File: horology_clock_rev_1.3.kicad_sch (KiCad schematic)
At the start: 49 parts, among them J1 Conn_01x36, J10 Conn_01x08, J11 Screw_Terminal_01x02, J12 Conn_01x02, J13 Conn_01x04, J14 Conn_01x10, J2 Conn_01x36, J3 Screw_Terminal_01x02, J4 Screw_Terminal_01x02, J5 Screw_Terminal_01x02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

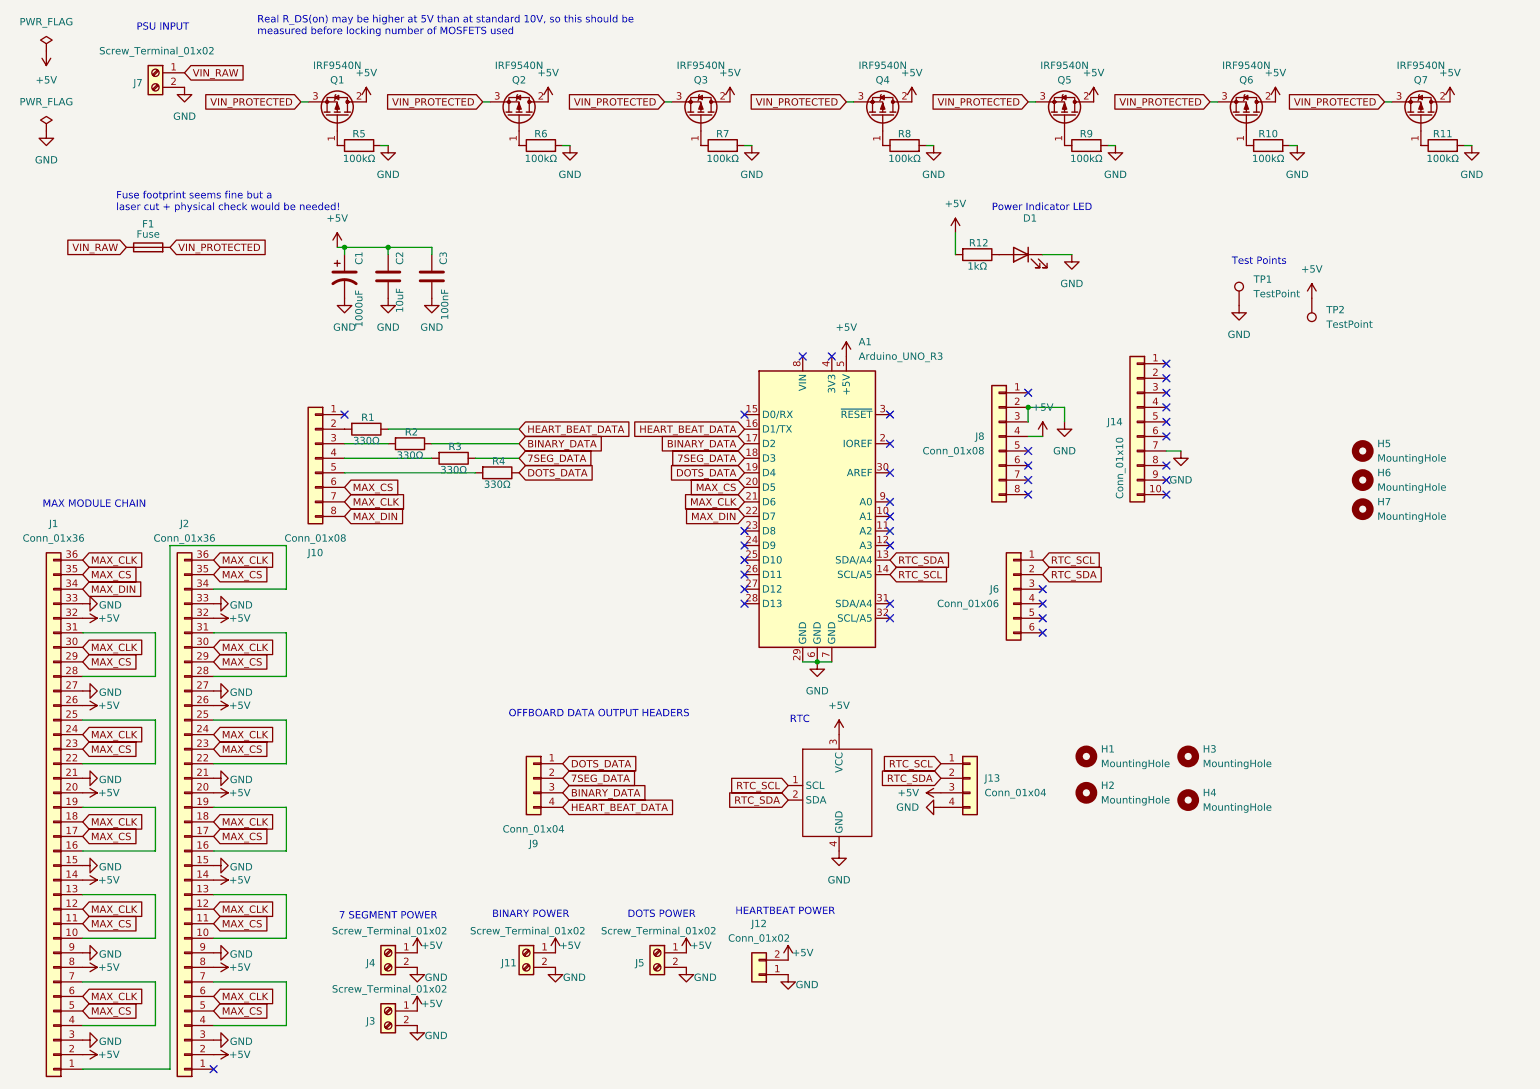
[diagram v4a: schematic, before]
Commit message: Moved Pin 1 to Pin 8 to avoid Serial Issues.
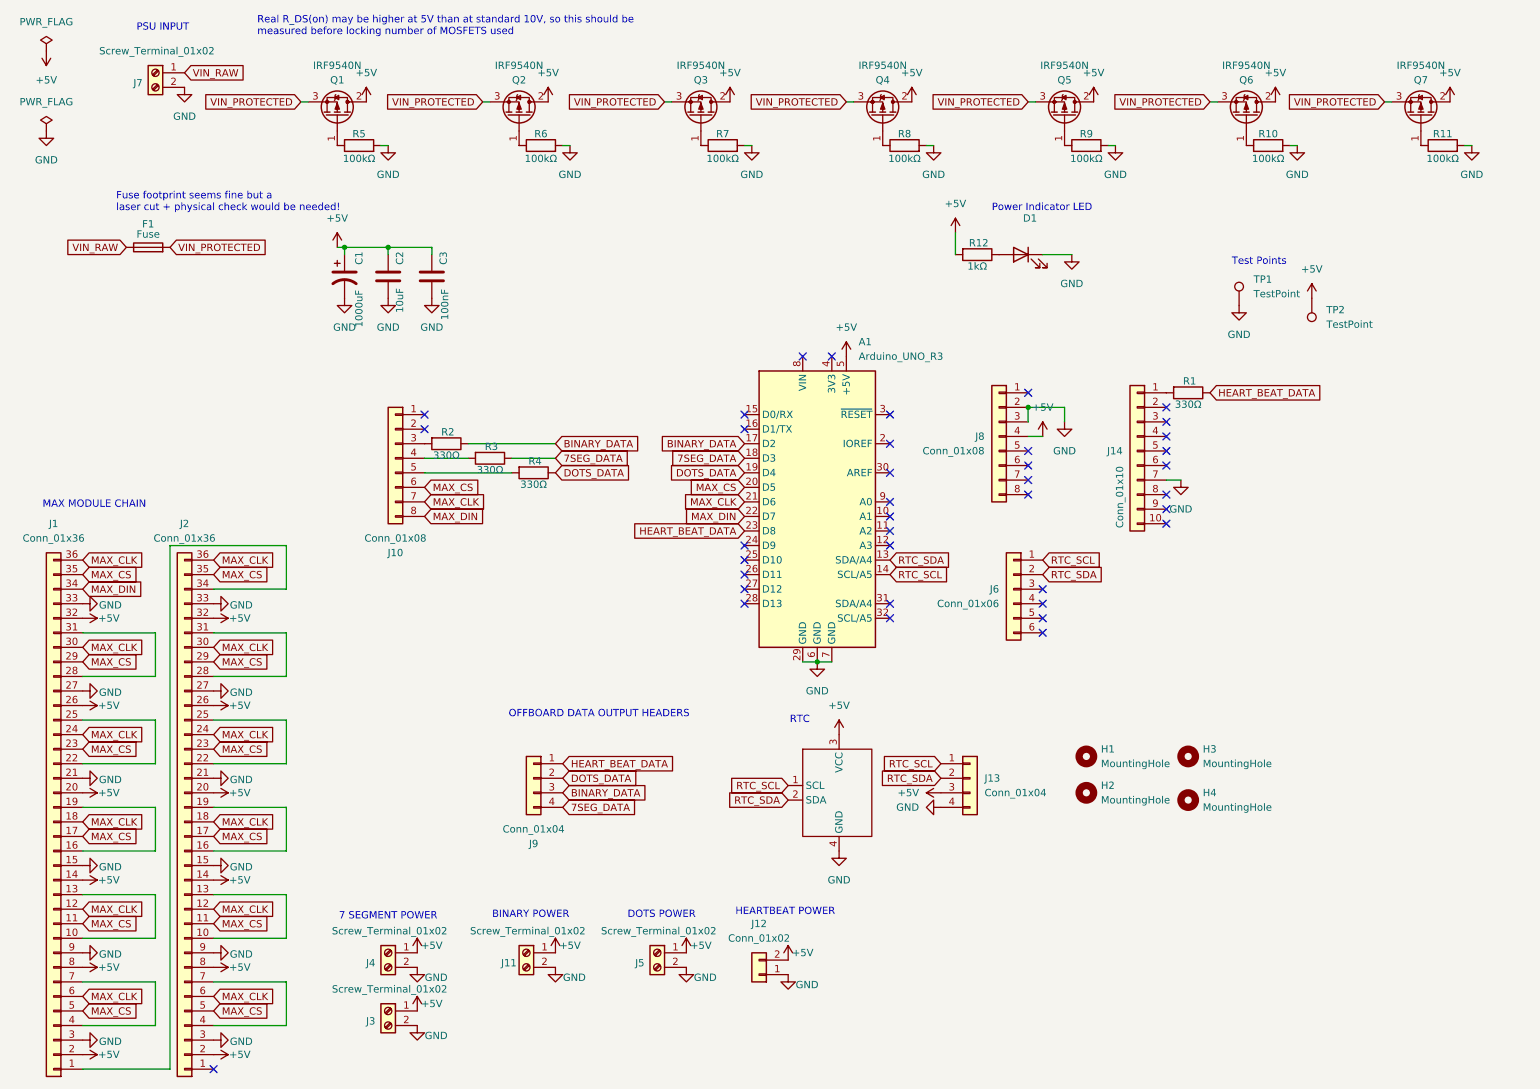
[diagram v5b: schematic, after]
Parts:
- removed H5, H6, H7: MountingHole, symbol Mechanical:MountingHole
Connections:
- net 7SEG_DATA: now also J9.4 (Pin_4); no longer J9.2 (Pin_2)
- net DOTS_DATA: now also J9.2 (Pin_2); no longer J9.1 (Pin_1)
- net HEART_BEAT_DATA: now also A1.23 (D8), J9.1 (Pin_1); no longer A1.16 (D1/TX), J9.4 (Pin_4)
- net at R1.2: now also J14.1 (3.3V); no longer J10.2 (Pin_2)
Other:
- moved on the sheet: J10, J14, R1, R2, R3, R4

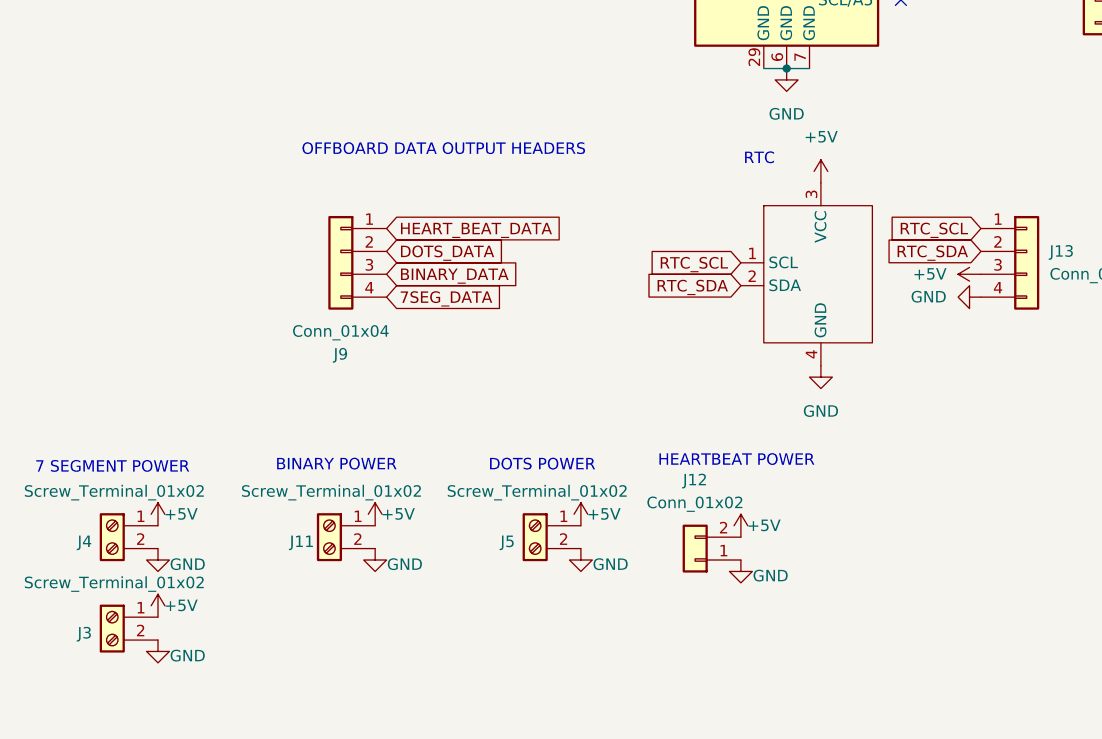
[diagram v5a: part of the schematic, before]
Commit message: Grouped Data and Power ouputs into close physical units.
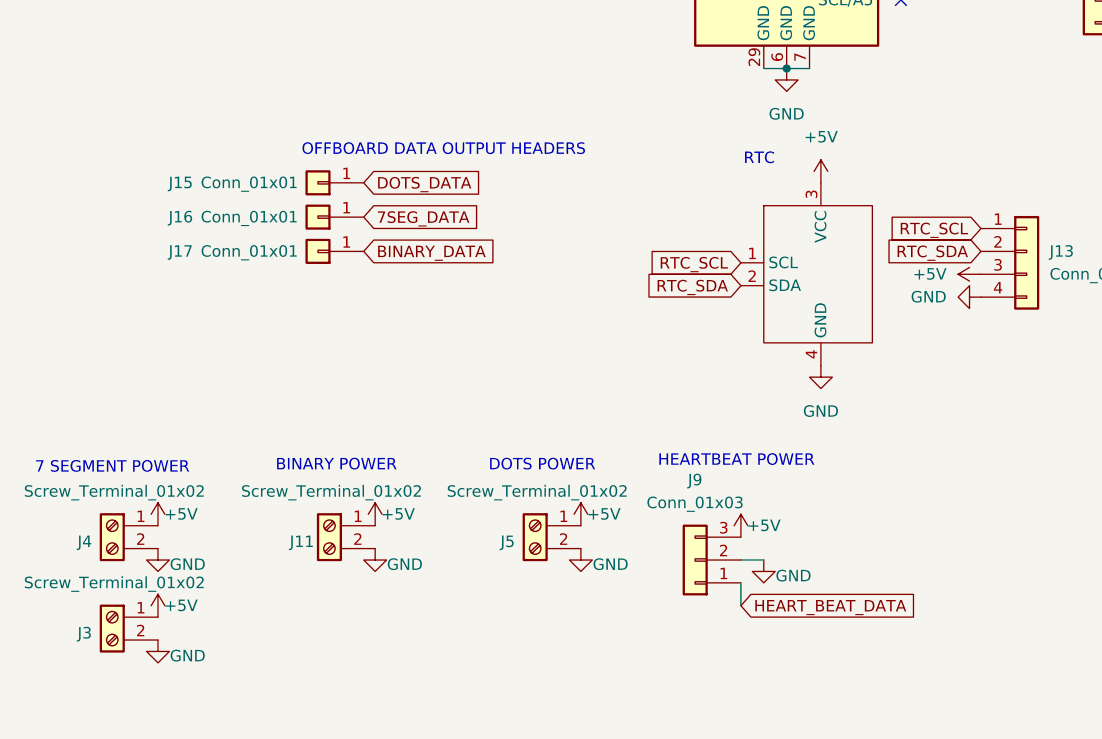
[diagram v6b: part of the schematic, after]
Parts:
- removed J12: Conn_01x02, Connector_PinHeader_2.54mm:PinHeader_1x02_P2.54mm_Vertical, symbol Connector_Generic:Conn_01x02
- removed J9: Conn_01x04, Connector_PinHeader_2.54mm:PinHeader_1x04_P2.54mm_Vertical, symbol Connector_Generic:Conn_01x04
- added J15, J16, J17: Conn_01x01, Connector_PinHeader_2.54mm:PinHeader_1x01_P2.54mm_Horizontal, symbol Connector_Generic:Conn_01x01
- added J9: Conn_01x03, Connector_PinHeader_2.54mm:PinHeader_1x03_P2.54mm_Horizontal, symbol Connector_Generic:Conn_01x03
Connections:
- net +5V: now also J9.3 (Pin_3)
- net 7SEG_DATA: now also J16.1 (Pin_1)
- net BINARY_DATA: now also J17.1 (Pin_1)
- net DOTS_DATA: now also J15.1 (Pin_1)
- net GND: now also J9.2 (Pin_2)
- net HEART_BEAT_DATA: now also J9.1 (Pin_1)

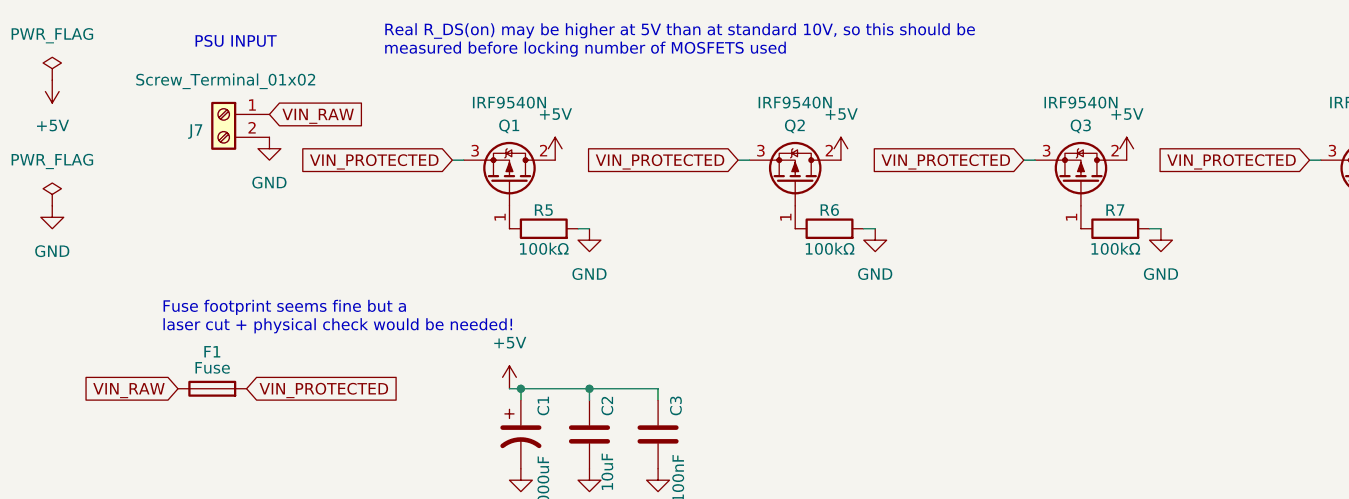
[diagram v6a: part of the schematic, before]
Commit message: Spaced the MOSFETs out around the Fuse for easy access with fat fingies.
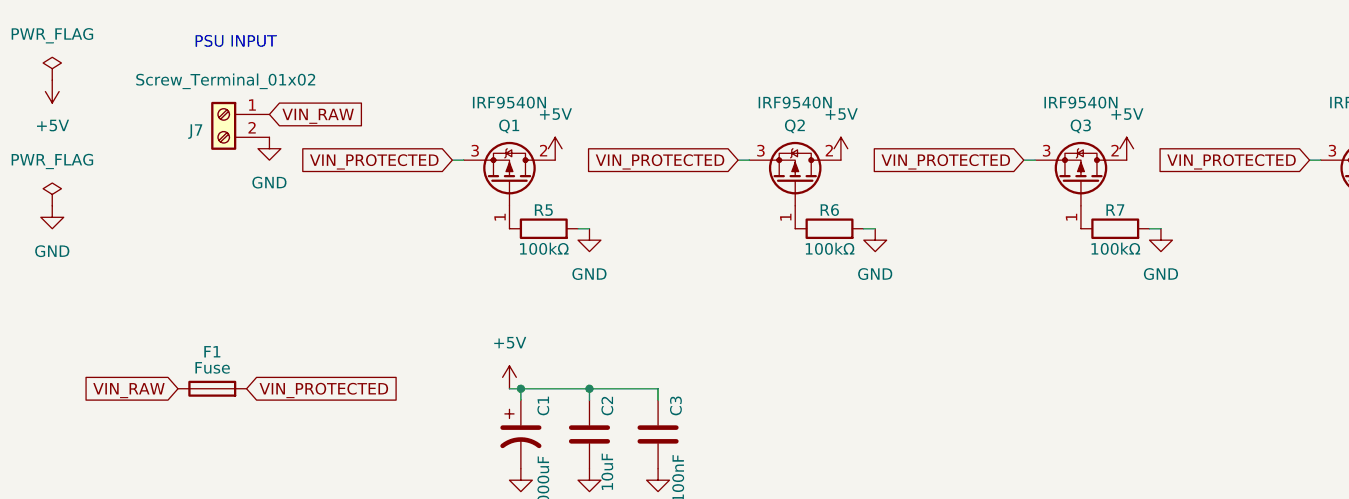
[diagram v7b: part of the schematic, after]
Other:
- note removed: "Fuse footprint seems fine but a laser cut + physical check would be needed!"
- note removed: "Real R_DS(on) may be higher at 5V than at standard 10V, so this should be measured before locking number of MOSFETS used"
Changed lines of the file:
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@@
-		)
-	)
-	(text "Real R_DS(on) may be higher at 5V than at standard 10V, so this should be \nmeasured before locking number of MOSFETS used"
-		(exclude_from_sim no)
-		(at 54.61 14.732 0)
-		(effects
-			(font
-				(size 1.27 1.27)
-			)
-			(justify left)
 		)
 	)
@@
 		)
 	)
-	(text "Fuse footprint seems fine but a \nlaser cut + physical check would be needed!"
-		(exclude_from_sim no)
-		(at 29.972 45.466 0)
-		(effects
-			(font
-				(size 1.27 1.27)
-			)
-			(justify left)
-		)
-	)

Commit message: Ready for Fab.
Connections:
- net GND: now also J7.1 (Pin_1); no longer J7.2 (Pin_2)
- net VIN_RAW: now also J7.2 (Pin_2); no longer J7.1 (Pin_1)
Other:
- moved on the sheet: J7
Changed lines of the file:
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@@
 	(symbol
 		(lib_id "Connector:Screw_Terminal_01x02")
-		(at 36.83 22.86 0)
-		(mirror y)
+		(at 36.83 25.4 180)
 		(unit 1)
 		(exclude_from_sim no)
@@
 		(dnp no)
 		(property "Reference" "J7"
-			(at 33.782 24.638 0)
+			(at 33.782 23.622 0)
 			(effects
 				(font
@@
 		)
 		(property "Value" "Screw_Terminal_01x02"
-			(at 37.084 19.05 0)
+			(at 38.1 18.542 0)
 			(effects
 				(font
@@
 		)
 		(property "Footprint" "TerminalBlock:TerminalBlock_MaiXu_MX126-5.0-02P_1x02_P5.00mm"
-			(at 36.83 22.86 0)
+			(at 36.83 25.4 0)
 			(effects
 				(font
@@
 		)
 		(property "Datasheet" "~"
-			(at 36.83 22.86 0)
+			(at 36.83 25.4 0)
 			(effects
 				(font
@@
 		)
 		(property "Description" "Generic screw terminal, single row, 01x02, script generated (kicad-library-utils/schlib/autogen/connector/)"
-			(at 36.83 22.86 0)
+			(at 36.83 25.4 0)
 			(effects
 				(font
